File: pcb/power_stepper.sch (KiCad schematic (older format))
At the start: 40 parts, among them J2 Screw_Terminal, U2 powerSTEP01

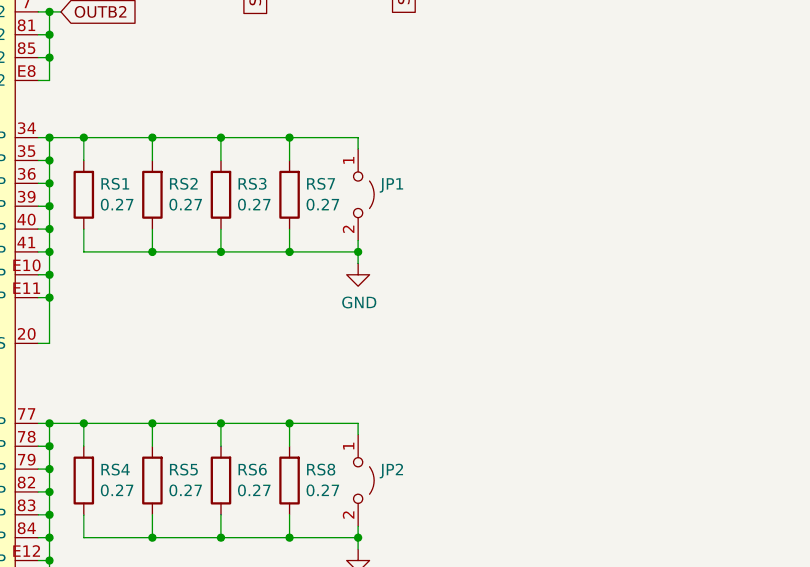
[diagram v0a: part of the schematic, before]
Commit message: connecting esp32 signals
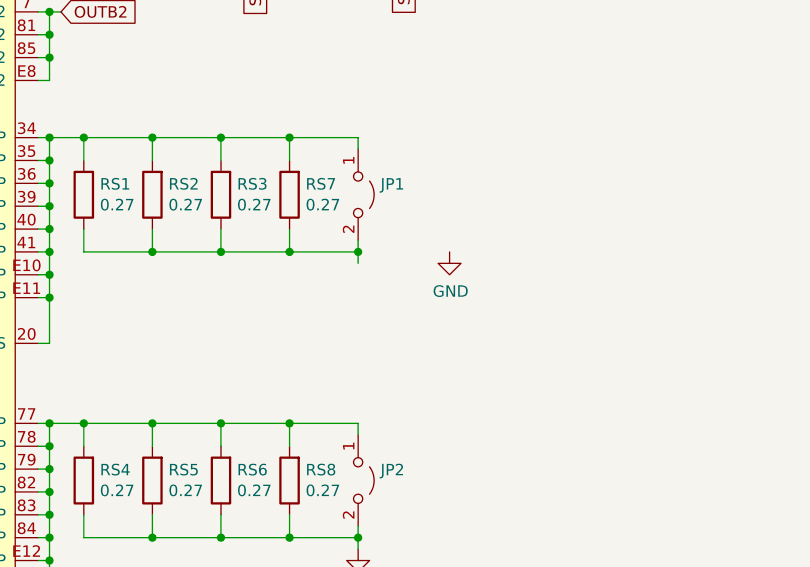
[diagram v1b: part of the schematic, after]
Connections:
- net GND: no longer JP1.2 (B), RS1.1, RS2.1, RS3.1, RS7.1
- new net: JP1.2 (B), RS1.1, RS2.1, RS3.1, RS7.1
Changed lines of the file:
@@
 L power:GND #PWR0126
 U 1 1 5BF8A45D
-P 5100 3450
-F 0 "#PWR0126" H 5100 3200 50  0001 C CNN
-F 1 "GND" H 5105 3277 50  0000 C CNN
-F 2 "" H 5100 3450 50  0001 C CNN
-F 3 "" H 5100 3450 50  0001 C CNN
-	1    5100 3450
+P 5500 3400
+F 0 "#PWR0126" H 5500 3150 50  0001 C CNN
+F 1 "GND" H 5505 3227 50  0000 C CNN
+F 2 "" H 5500 3400 50  0001 C CNN
+F 3 "" H 5500 3400 50  0001 C CNN
+	1    5500 3400
 	1    0    0    -1
 $EndComp

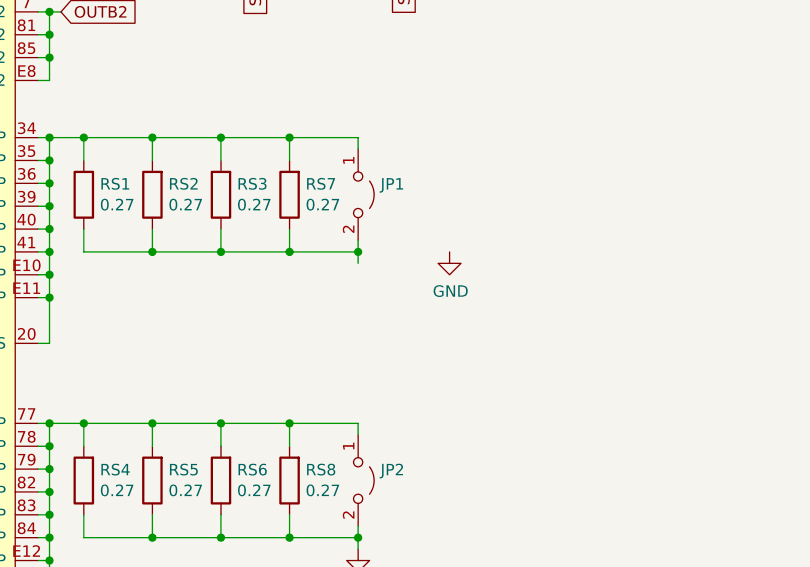
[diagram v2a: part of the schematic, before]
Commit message: led drive transistors
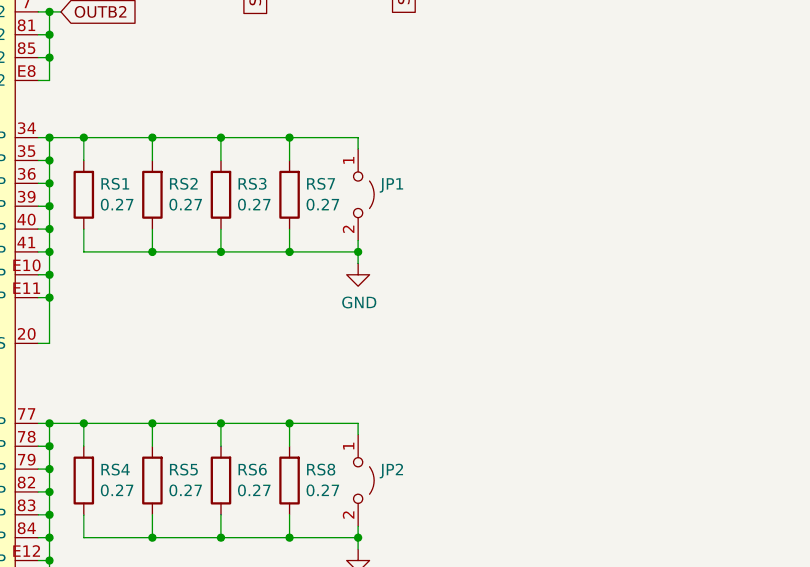
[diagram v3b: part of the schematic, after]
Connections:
- net GND: now also JP1.2 (B), RS1.1, RS2.1, RS3.1, RS7.1
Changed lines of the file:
@@
 EESchema Schematic File Version 4
 LIBS:keep_breathing_ctrl-cache
-EELAYER 26 0
+EELAYER 30 0
 EELAYER END
 $Descr A4 11693 8268
@@
 L power:GND #PWR0126
 U 1 1 5BF8A45D
-P 5500 3400
-F 0 "#PWR0126" H 5500 3150 50  0001 C CNN
-F 1 "GND" H 5505 3227 50  0000 C CNN
-F 2 "" H 5500 3400 50  0001 C CNN
-F 3 "" H 5500 3400 50  0001 C CNN
-	1    5500 3400
-	1    0    0    -1
-$EndComp
+P 5100 3450
+F 0 "#PWR0126" H 5100 3200 50  0001 C CNN
+F 1 "GND" H 5105 3277 50  0000 C CNN
+F 2 "" H 5100 3450 50  0001 C CNN
+F 3 "" H 5100 3450 50  0001 C CNN
+	1    5100 3450
+	1    0    0    -1
+$EndComp

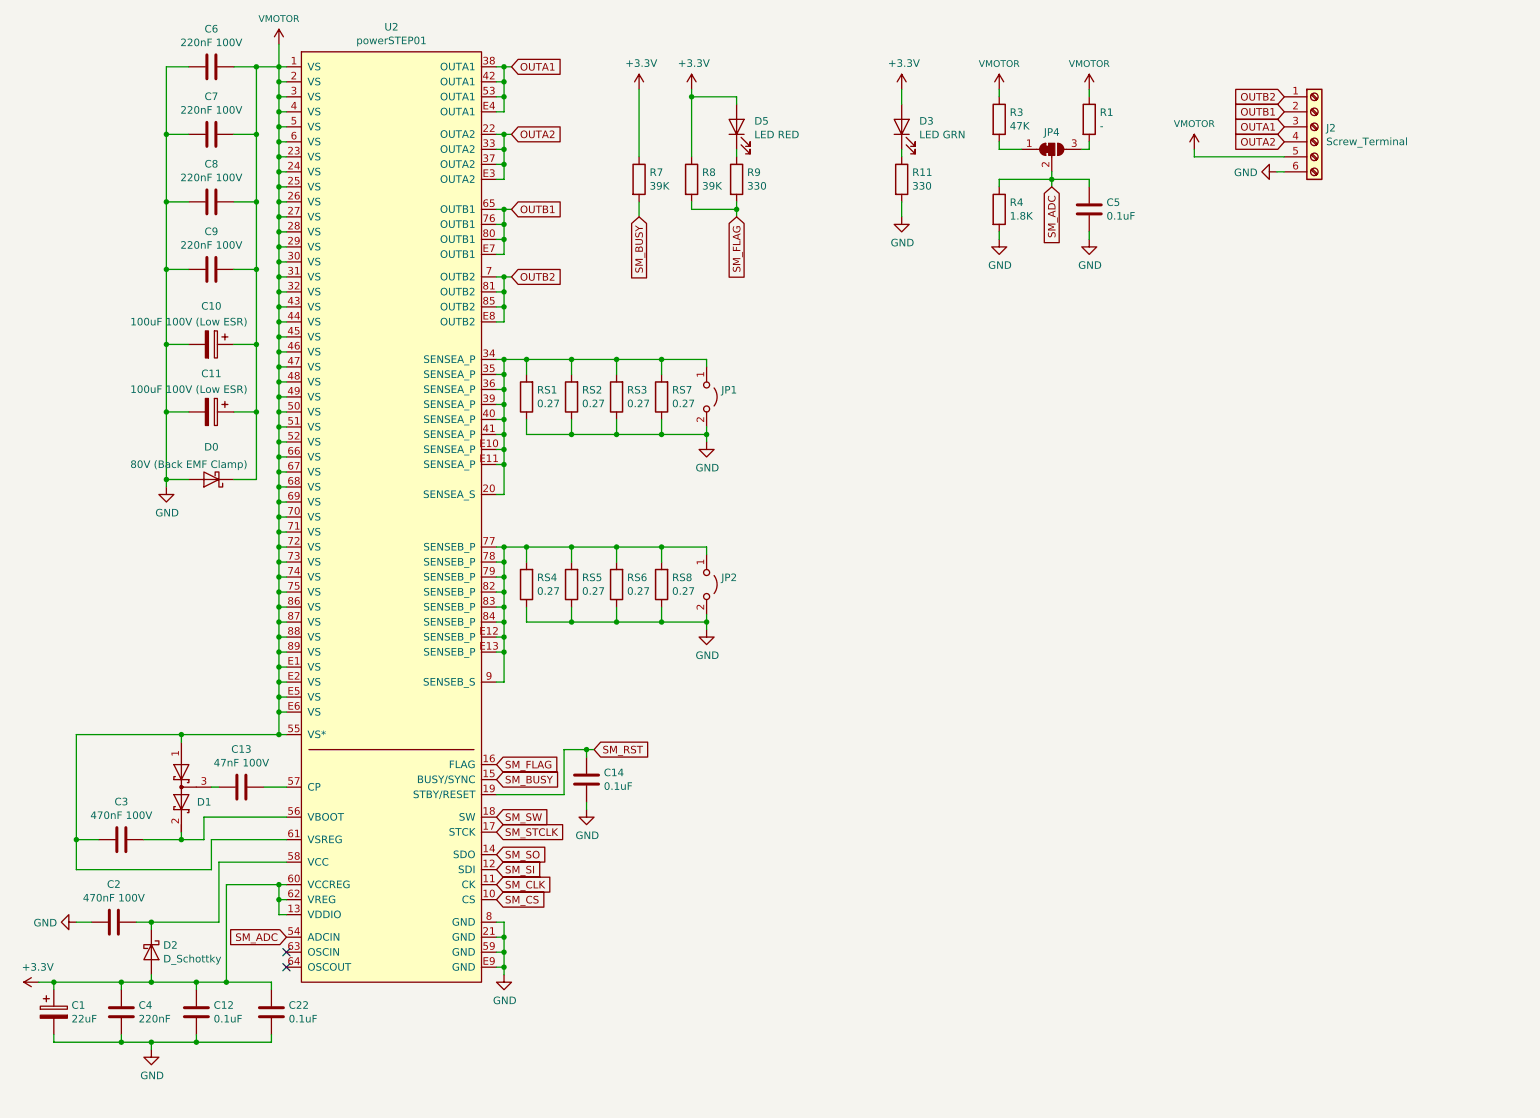
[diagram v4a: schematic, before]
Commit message: GND isolated for motor driver
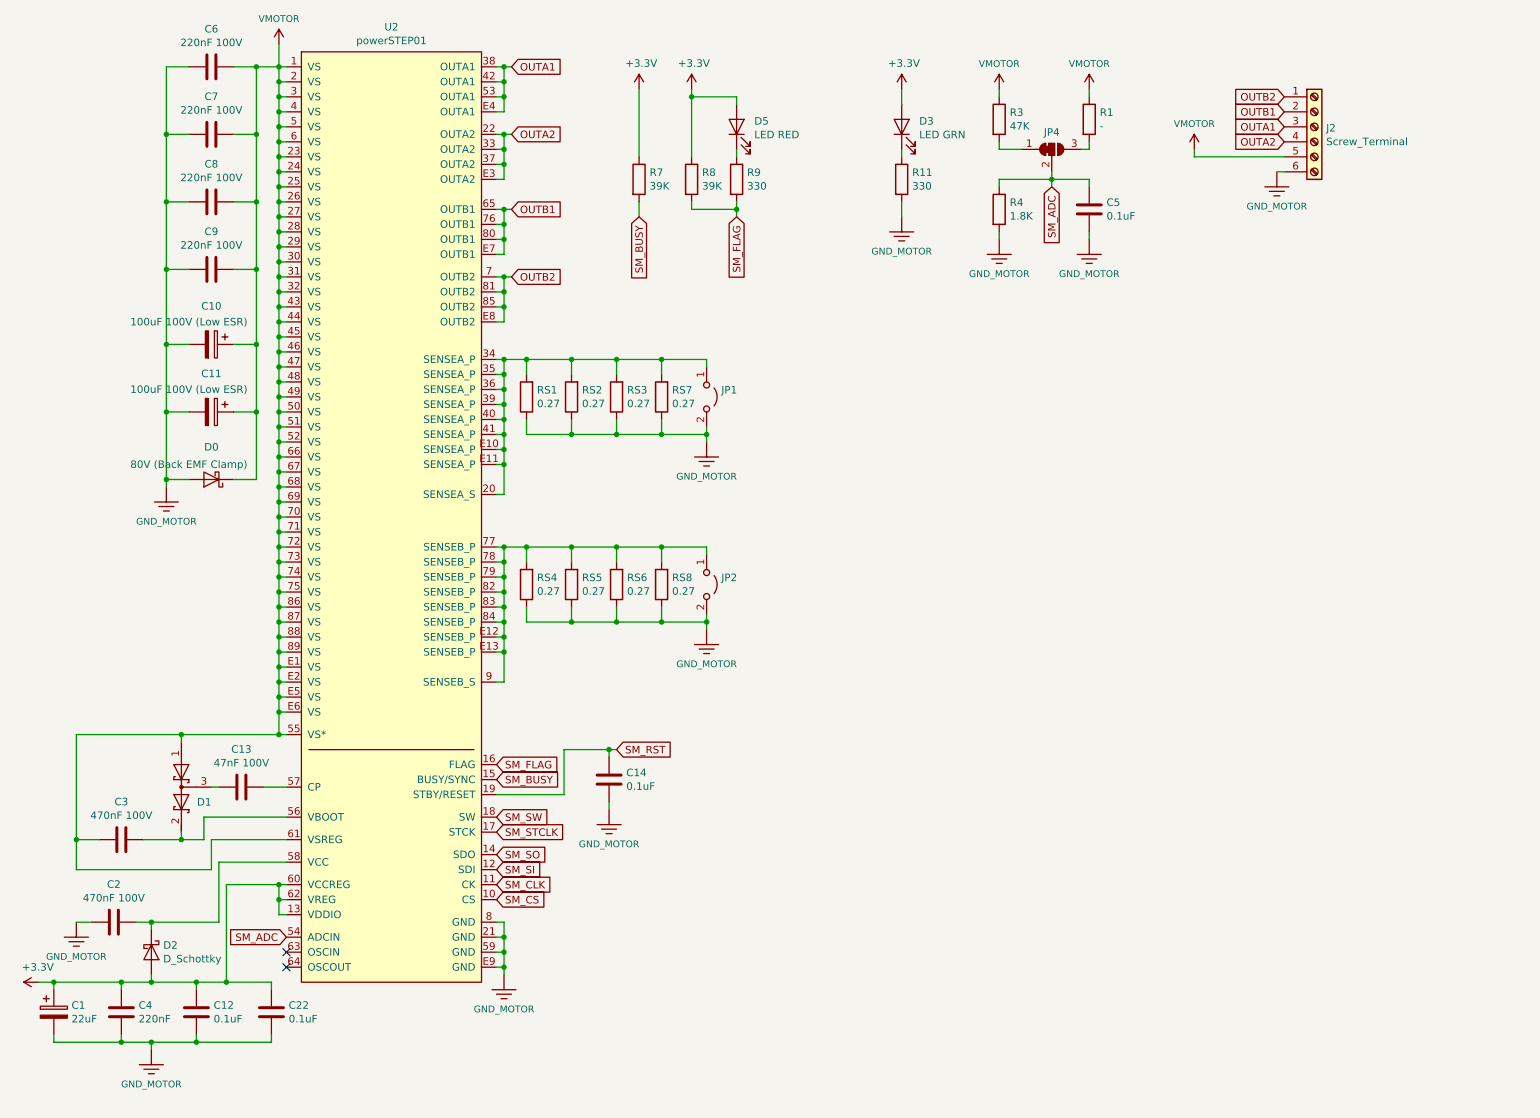
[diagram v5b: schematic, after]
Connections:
- net GND renamed 3.3V
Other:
- moved on the sheet: C14
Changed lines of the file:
@@
 EESchema Schematic File Version 4
+LIBS:keep_breathing_ctrl-cache
 EELAYER 30 0
 EELAYER END
@@
 Wire Wire Line
 	1500 1400 1500 1850
-$Comp
-L power:GND #PWR0113
-U 1 1 5B80B165
-P 1500 3750
-F 0 "#PWR0113" H 1500 3500 50  0001 C CNN
-F 1 "GND" H 1505 3577 50  0000 C CNN
-F 2 "" H 1500 3750 50  0001 C CNN
-F 3 "" H 1500 3750 50  0001 C CNN
-	1    1500 3750
-	1    0    0    -1
-$EndComp
 Connection ~ 1500 3250
 NoConn ~ 2300 6950
@@
 Text GLabel 3700 6500 2    50   Input ~ 0
 SM_CS
-$Comp
-L power:GND #PWR0114
-U 1 1 5B83F3E9
-P 3750 7000
-F 0 "#PWR0114" H 3750 6750 50  0001 C CNN
-F 1 "GND" H 3755 6827 50  0000 C CNN
-F 2 "" H 3750 7000 50  0001 C CNN
-F 3 "" H 3750 7000 50  0001 C CNN
-	1    3750 7000
-	1    0    0    -1
-$EndComp
 Wire Wire Line
 	3750 7000 3750 6950
@@
 Text GLabel 3700 6050 2    50   Input ~ 0
 SM_STCLK
-Text GLabel 4350 5500 2    50   Input ~ 0
+Text GLabel 4500 5500 2    50   Input ~ 0
 SM_RST
 $Comp
 L Device:C C14
 U 1 1 5B8E4778
-P 4300 5700
-F 0 "C14" H 4415 5746 50  0000 L CNN
-F 1 "0.1uF" H 4415 5655 50  0000 L CNN
-F 2 "Capacitor_SMD:C_0603_1608Metric" H 4338 5550 50  0001 C CNN
-F 3 "~" H 4300 5700 50  0001 C CNN
-	1    4300 5700
+P 4450 5700
+F 0 "C14" H 4565 5746 50  0000 L CNN
+F 1 "0.1uF" H 4565 5655 50  0000 L CNN
+F 2 "Capacitor_SMD:C_0603_1608Metric" H 4488 5550 50  0001 C CNN
+F 3 "~" H 4450 5700 50  0001 C CNN
+	1    4450 5700
 	1    0    0    -1
 $EndComp
 Wire Wire Line
 	3700 5800 4150 5800
-$Comp
-L power:GND #PWR0115
-U 1 1 5B90AB63
-P 4300 5900
-F 0 "#PWR0115" H 4300 5650 50  0001 C CNN
-F 1 "GND" H 4305 5727 50  0000 C CNN
-F 2 "" H 4300 5900 50  0001 C CNN
-F 3 "" H 4300 5900 50  0001 C CNN
-	1    4300 5900
-	1    0    0    -1
-$EndComp
 $Comp
 L Device:D_Schottky_x2_Serial_AKC D1
@@
 Wire Wire Line
 	2250 5250 2250 5400
-$Comp
-L power:GND #PWR0118
-U 1 1 5BC8FD02
-P 8900 1650
-F 0 "#PWR0118" H 8900 1400 50  0001 C CNN
-F 1 "GND" V 8905 1522 50  0000 R CNN
-F 2 "" H 8900 1650 50  0001 C CNN
-F 3 "" H 8900 1650 50  0001 C CNN
-	1    8900 1650
-	0    1    1    0
-$EndComp
 Text GLabel 5300 1950 3    50   Input ~ 0
 SM_FLAG
@@
 	0    -1   -1   0
 $EndComp
-$Comp
-L power:GND #PWR0121
-U 1 1 5BD16EC2
-P 5100 4700
-F 0 "#PWR0121" H 5100 4450 50  0001 C CNN
-F 1 "GND" H 5105 4527 50  0000 C CNN
-F 2 "" H 5100 4700 50  0001 C CNN
-F 3 "" H 5100 4700 50  0001 C CNN
-	1    5100 4700
-	1    0    0    -1
-$EndComp
 Wire Wire Line
 	3900 4250 3900 4150
@@
 	1    0    0    -1
 $EndComp
-$Comp
-L power:GND #PWR0125
-U 1 1 5BEF953F
-P 6400 1950
-F 0 "#PWR0125" H 6400 1700 50  0001 C CNN
-F 1 "GND" H 6405 1777 50  0000 C CNN
-F 2 "" H 6400 1950 50  0001 C CNN
-F 3 "" H 6400 1950 50  0001 C CNN
-	1    6400 1950
-	1    0    0    -1
-$EndComp
 Wire Wire Line
 	6400 1500 6400 1550
@@
 Wire Wire Line
 	6400 1850 6400 1950
-$Comp
-L power:GND #PWR0126
-U 1 1 5BF8A45D
-P 5100 3450
-F 0 "#PWR0126" H 5100 3200 50  0001 C CNN
-F 1 "GND" H 5105 3277 50  0000 C CNN
-F 2 "" H 5100 3450 50  0001 C CNN
-F 3 "" H 5100 3450 50  0001 C CNN
-	1    5100 3450
-	1    0    0    -1
-$EndComp
 Wire Wire Line
 	3900 3000 3900 2900
@@
 	0    1    1    0
 $EndComp
-$Comp
-L power:GND #PWR0127
-U 1 1 5C3B575A
-P 900 6650
-F 0 "#PWR0127" H 900 6400 50  0001 C CNN
-F 1 "GND" V 905 6522 50  0000 R CNN
-F 2 "" H 900 6650 50  0001 C CNN
-F 3 "" H 900 6650 50  0001 C CNN
-	1    900  6650
-	0    1    1    0
-$EndComp
 Wire Wire Line
 	900  6650 1000 6650
@@
 	1400 7050 1700 7050
 Connection ~ 1400 7450
-$Comp
-L power:GND #PWR0129
-U 1 1 5C9A5DB1
-P 1400 7500
-F 0 "#PWR0129" H 1400 7250 50  0001 C CNN
-F 1 "GND" H 1405 7327 50  0000 C CNN
-F 2 "" H 1400 7500 50  0001 C CNN
-F 3 "" H 1400 7500 50  0001 C CNN
-	1    1400 7500
-	1    0    0    -1
-$EndComp
 Wire Wire Line
 	1400 7500 1400 7450
@@
 Wire Wire Line
 	7400 1700 7400 1750
-$Comp
-L power:GND #PWR0136
-U 1 1 5C8D742C
-P 7650 2100
-F 0 "#PWR0136" H 7650 1850 50  0001 C CNN
-F 1 "GND" H 7655 1927 50  0000 C CNN
-F 2 "" H 7650 2100 50  0001 C CNN
-F 3 "" H 7650 2100 50  0001 C CNN
-	1    7650 2100
-	1    0    0    -1
-$EndComp
 Wire Wire Line
 	7200 1500 7050 1500
@@
 Wire Wire Line
 	7050 1700 7050 1750
-$Comp
-L power:GND #PWR0128
-U 1 1 5CB6FDFC
-P 7050 2100
-F 0 "#PWR0128" H 7050 1850 50  0001 C CNN
-F 1 "GND" H 7055 1927 50  0000 C CNN
-F 2 "" H 7050 2100 50  0001 C CNN
-F 3 "" H 7050 2100 50  0001 C CNN
-	1    7050 2100
-	1    0    0    -1
-$EndComp
 Wire Wire Line
 	7050 2100 7050 2050
@@
 	7650 2100 7650 2050
 Wire Wire Line
-	4150 5500 4300 5500
-Wire Wire Line
-	4300 5550 4300 5500
-Connection ~ 4300 5500
-Wire Wire Line
-	4300 5500 4350 5500
-Wire Wire Line
-	4300 5900 4300 5850
+	4150 5500 4450 5500
+Wire Wire Line
+	4450 5550 4450 5500
+Connection ~ 4450 5500
+Wire Wire Line
+	4450 5500 4500 5500
+Wire Wire Line
+	4450 5900 4450 5850
 Wire Wire Line
 	4150 5500 4150 5800
@@
 	1    0    0    -1
 $EndComp
+$Comp
+L ventilator-PowerSymbols:GND_MOTOR #GND?
+U 1 1 5E9A6CBA
+P 5100 4700
+F 0 "#GND?" H 5150 4650 45  0001 L BNN
+F 1 "GND_MOTOR" H 5100 4470 45  0000 C CNN
+F 2 "XXX-00000" H 5100 4375 60  0001 C CNN
+F 3 "" H 5100 4600 60  0001 C CNN
+	1    5100 4700
+	1    0    0    -1
+$EndComp
+$Comp
+L ventilator-PowerSymbols:GND_MOTOR #GND?
+U 1 1 5E9AAE09
+P 5100 3450
+F 0 "#GND?" H 5150 3400 45  0001 L BNN
+F 1 "GND_MOTOR" H 5100 3220 45  0000 C CNN
+F 2 "XXX-00000" H 5100 3125 60  0001 C CNN
+F 3 "" H 5100 3350 60  0001 C CNN
+	1    5100 3450
+	1    0    0    -1
+$EndComp
+$Comp
+L ventilator-PowerSymbols:GND_MOTOR #GND?
+U 1 1 5E9CBE33
+P 6400 1950
+F 0 "#GND?" H 6450 1900 45  0001 L BNN
+F 1 "GND_MOTOR" H 6400 1720 45  0000 C CNN
+F 2 "XXX-00000" H 6400 1625 60  0001 C CNN
+F 3 "" H 6400 1850 60  0001 C CNN
+	1    6400 1950
+	1    0    0    -1
+$EndComp
+$Comp
+L ventilator-PowerSymbols:GND_MOTOR #GND?
+U 1 1 5E9CCFE8
+P 7650 2100
+F 0 "#GND?" H 7700 2050 45  0001 L BNN
+F 1 "GND_MOTOR" H 7650 1870 45  0000 C CNN
+F 2 "XXX-00000" H 7650 1775 60  0001 C CNN
+F 3 "" H 7650 2000 60  0001 C CNN
+	1    7650 2100
+	1    0    0    -1
+$EndComp
+$Comp
+L ventilator-PowerSymbols:GND_MOTOR #GND?
+U 1 1 5E9CED1E
+P 7050 2100
+F 0 "#GND?" H 7100 2050 45  0001 L BNN
+F 1 "GND_MOTOR" H 7050 1870 45  0000 C CNN
+F 2 "XXX-00000" H 7050 1775 60  0001 C CNN
+F 3 "" H 7050 2000 60  0001 C CNN
+	1    7050 2100
+	1    0    0    -1
+$EndComp
+$Comp
+L ventilator-PowerSymbols:GND_MOTOR #GND?
+U 1 1 5EA19716
+P 8900 1650
+F 0 "#GND?" H 8950 1600 45  0001 L BNN
+F 1 "GND_MOTOR" H 8900 1420 45  0000 C CNN
+F 2 "XXX-00000" H 8900 1325 60  0001 C CNN
+F 3 "" H 8900 1550 60  0001 C CNN
+	1    8900 1650
+	1    0    0    -1
+$EndComp
+$Comp
+L ventilator-PowerSymbols:GND_MOTOR #GND?
+U 1 1 5EA38790
+P 1500 3750
+F 0 "#GND?" H 1550 3700 45  0001 L BNN
+F 1 "GND_MOTOR" H 1500 3520 45  0000 C CNN
+F 2 "XXX-00000" H 1500 3425 60  0001 C CNN
+F 3 "" H 1500 3650 60  0001 C CNN
+	1    1500 3750
+	1    0    0    -1
+$EndComp
+$Comp
+L ventilator-PowerSymbols:GND_MOTOR #GND?
+U 1 1 5EA3E7A5
+P 1400 7500
+F 0 "#GND?" H 1450 7450 45  0001 L BNN
+F 1 "GND_MOTOR" H 1400 7270 45  0000 C CNN
+F 2 "XXX-00000" H 1400 7175 60  0001 C CNN
+F 3 "" H 1400 7400 60  0001 C CNN
+	1    1400 7500
+	1    0    0    -1
+$EndComp
+$Comp
+L ventilator-PowerSymbols:GND_MOTOR #GND?
+U 1 1 5EA3F6C2
+P 900 6650
+F 0 "#GND?" H 950 6600 45  0001 L BNN
+F 1 "GND_MOTOR" H 900 6420 45  0000 C CNN
+F 2 "XXX-00000" H 900 6325 60  0001 C CNN
+F 3 "" H 900 6550 60  0001 C CNN
+	1    900  6650
+	1    0    0    -1
+$EndComp
+$Comp
+L ventilator-PowerSymbols:GND_MOTOR #GND?
+U 1 1 5EA3FDD5
+P 3750 7000
+F 0 "#GND?" H 3800 6950 45  0001 L BNN
+F 1 "GND_MOTOR" H 3750 6770 45  0000 C CNN
+F 2 "XXX-00000" H 3750 6675 60  0001 C CNN
+F 3 "" H 3750 6900 60  0001 C CNN
+	1    3750 7000
+	1    0    0    -1
+$EndComp
+$Comp
+L ventilator-PowerSymbols:GND_MOTOR #GND?
+U 1 1 5EA40977
+P 4450 5900
+F 0 "#GND?" H 4500 5850 45  0001 L BNN
+F 1 "GND_MOTOR" H 4450 5670 45  0000 C CNN
+F 2 "XXX-00000" H 4450 5575 60  0001 C CNN
+F 3 "" H 4450 5800 60  0001 C CNN
+	1    4450 5900
+	1    0    0    -1
+$EndComp
